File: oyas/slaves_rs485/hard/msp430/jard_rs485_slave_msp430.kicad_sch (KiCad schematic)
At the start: 59 parts, among them J1 POWER, J5 Prog MSP, U1 BPC_Alim3_3V, U1 MAX485E, U2 MSP430F1232IDW, Y1 8MHz

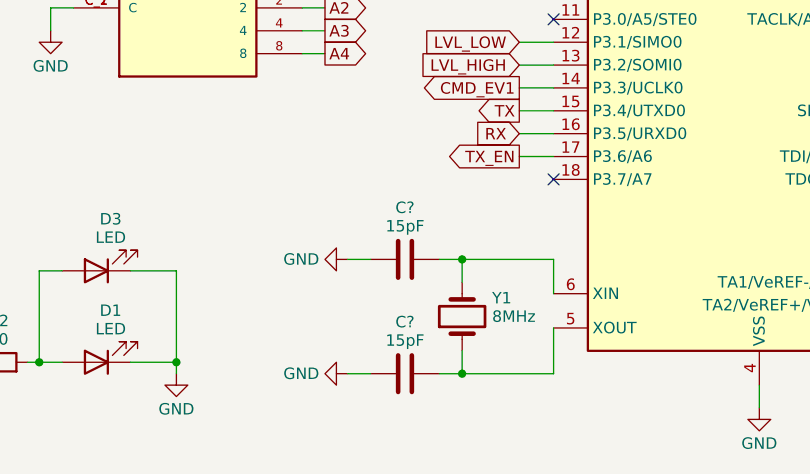
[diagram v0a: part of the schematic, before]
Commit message: Correction valeurs des capas du quartz
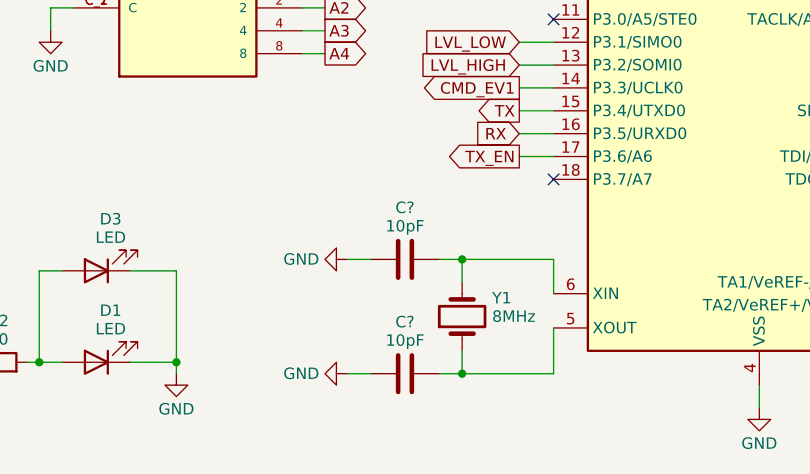
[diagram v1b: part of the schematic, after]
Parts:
- C? (x2): value 15pF -> 10pF
- Y1: Farnel 4235681 -> 4242855; RefFab ABM8AAIG-8.000MHZ-V2R-T -> ABM8AAIG-8.000MHZ-V2R-T3
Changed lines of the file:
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@@
       (effects (font (size 1.27 1.27)))
     )
-    (property "Value" "15pF" (at 95.25 180.459 90)
+    (property "Value" "10pF" (at 95.25 180.459 90)
       (effects (font (size 1.27 1.27)))
     )
@@
       (effects (font (size 1.27 1.27)) hide)
     )
-    (property "Farnel" "4235681" (at 95.25 177.8 0)
-      (effects (font (size 1.27 1.27)) hide)
-    )
-    (property "RefFab" "ABM8AAIG-8.000MHZ-V2R-T" (at 104.9274 179.848 90)
+    (property "Farnel" "4242855" (at 95.25 177.8 0)
+      (effects (font (size 1.27 1.27)) hide)
+    )
+    (property "RefFab" "ABM8AAIG-8.000MHZ-V2R-T3" (at 104.9274 179.848 90)
       (effects (font (size 1.27 1.27)) (justify right) hide)
     )
@@
       (effects (font (size 1.27 1.27)))
     )
-    (property "Value" "15pF" (at 95.25 167.759 90)
-      (effects (font (size 1.27 1.27)))
-    )
+    (property "Value" "10pF" (at 95.25 167.759 90)
+      (effects (font (size 1.27 1.27)))
+    )

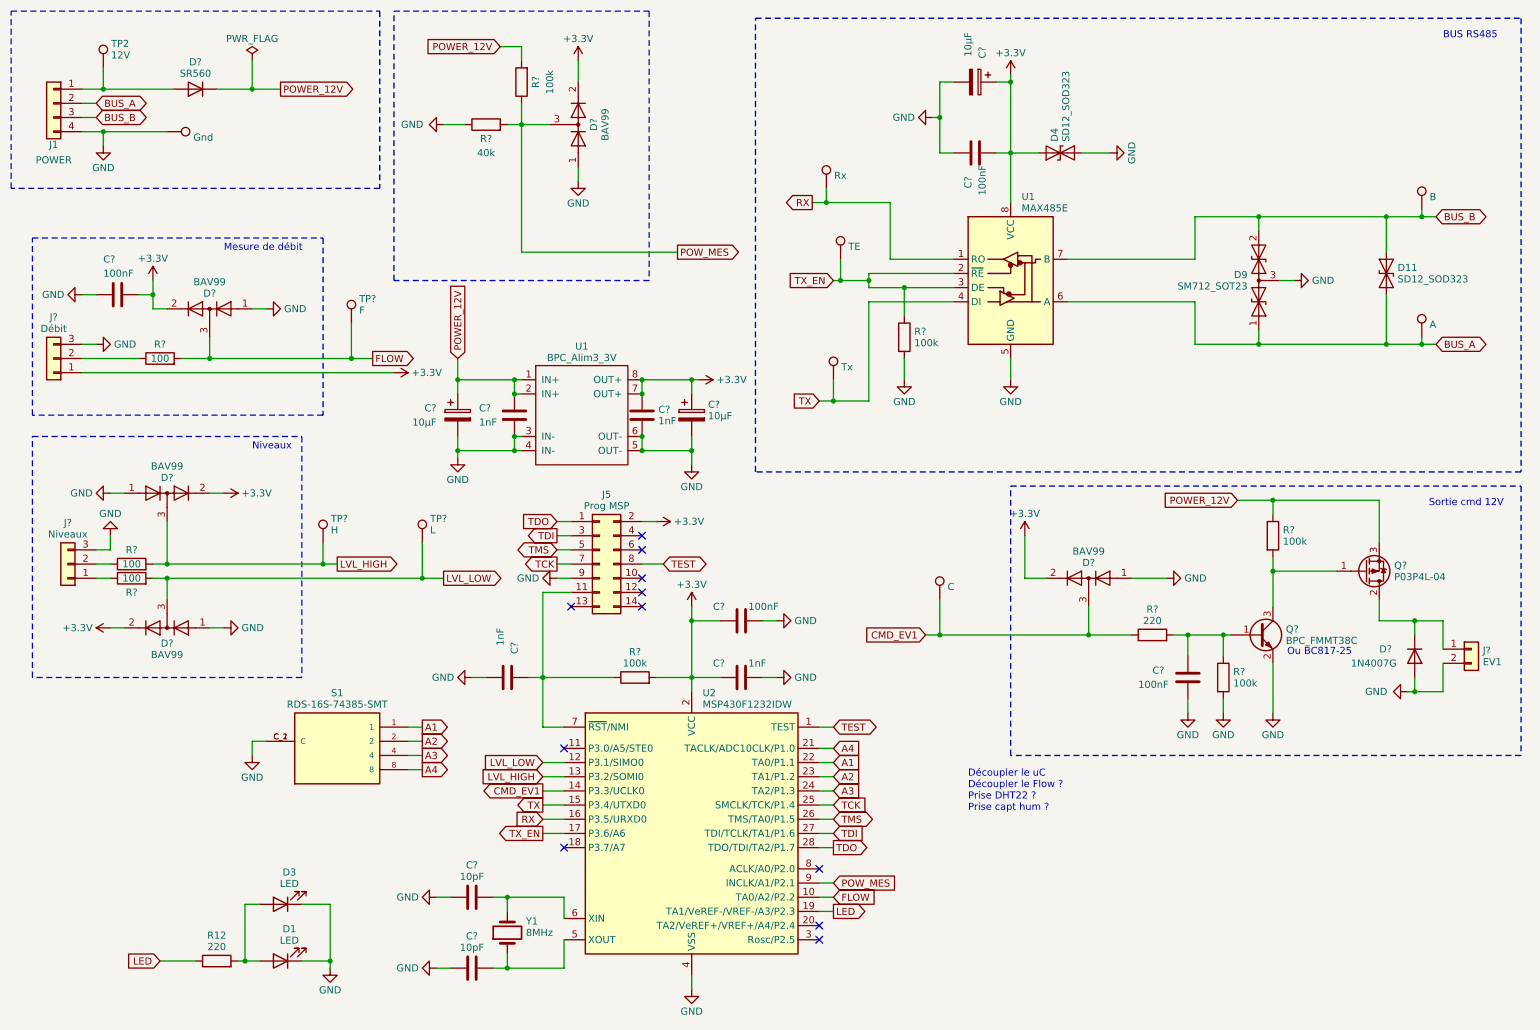
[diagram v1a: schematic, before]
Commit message: Corrections sur la carte Rev A MSP430
- Pas de pullup interne ds MSP430
- Correction sérigraphie et empreinte connecteur de PROG
- Décalage LED
- Suppression de l'entrée débit
- Empreinte des doides TVS et des capas pour être soudables à la main
- Empreinte D12 horizontale
- C8 et C10 en 805 au lieu de 603
- Grossissement de la sérigraphie de version
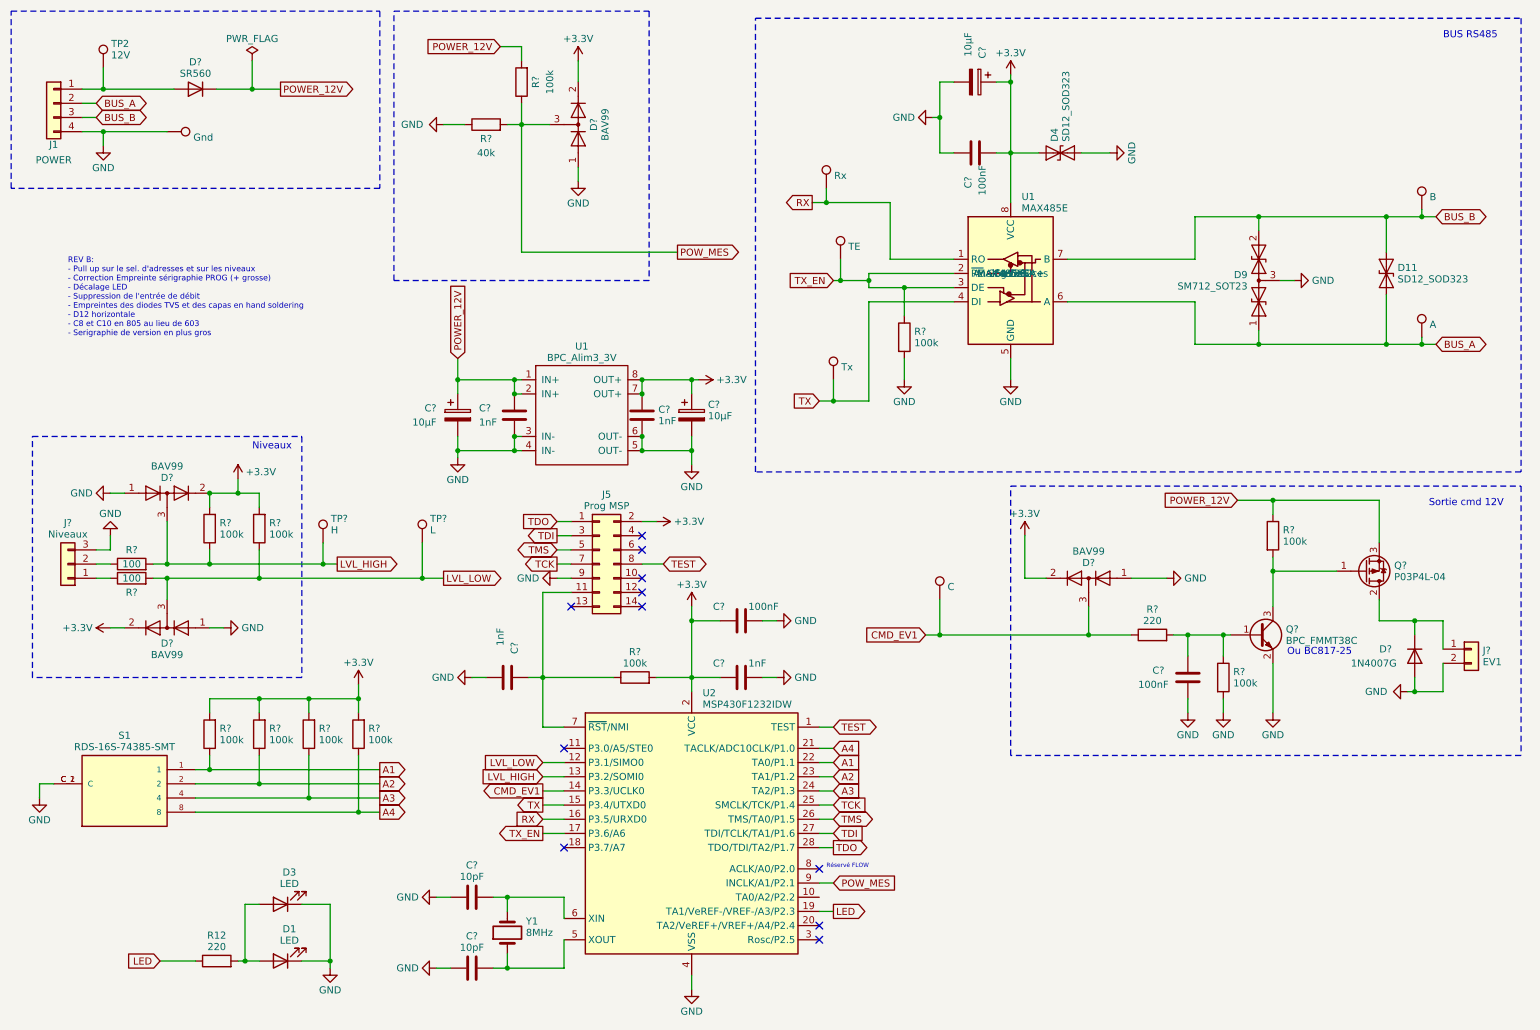
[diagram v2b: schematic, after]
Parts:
- removed C?: 100nF, Capacitor_SMD:C_0805_2012Metric, symbol Device:C
- removed D?: BAV99, Package_TO_SOT_SMD:SOT-23, symbol Diode:BAV99
- removed J?: Débit, TerminalBlock_Phoenix:TerminalBlock_Phoenix_MPT-0,5-3-2.54_1x03_P2.54mm_Horizontal, symbol Connector_Generic:Conn_01x03
- removed R?: 100, Resistor_SMD:R_0805_2012Metric_Pad1.20x1.40mm_HandSolder, symbol Device:R
- removed TP?: F, TestPoint:TestPoint_Pad_D1.0mm, symbol Connector:TestPoint
- added R? (x6): 100k, Resistor_SMD:R_0805_2012Metric_Pad1.20x1.40mm_HandSolder, symbol Device:R
- C? (x6): footprint Capacitor_SMD:C_0805_2012Metric -> Capacitor_SMD:C_0805_2012Metric_Pad1.18x1.45mm_HandSolder
- C? (x2): footprint Capacitor_SMD:C_0603_1608Metric -> Capacitor_SMD:C_0805_2012Metric_Pad1.18x1.45mm_HandSolder
- D11, D4: footprint Diode_SMD:D_SOD-323 -> Diode_SMD:D_SOD-323_HandSoldering
- D?: footprint Diode_THT:D_A-405_P5.08mm_Vertical_KathodeUp -> Diode_THT:D_A-405_P7.62mm_Horizontal
- S1: Price 2,76 -> None
- U1: Fabricant (none) -> Analog Devices; Fournisseur (none) -> Farnell; RefFabricant (none) -> MAX485ESA+; RefFournisseur (none) -> 2519382
- Y1: Fabricant (none) -> Abracon; Fournisseur (none) -> Farnell; RefFabricant (none) -> ABM8AAIG-8.000MHZ-V2R-T3; RefFournisseur (none) -> 4242855
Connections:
- net +3.3V: now also R?.2, R?.2, R?.2, R?.2, R?.2, R?.2
- net A1: now also R?.1
- net A2: now also R?.1
- net A3: now also R?.1
- net A4: now also R?.1
- net LVL_HIGH: now also R?.1
- net LVL_LOW: now also R?.1
- net FLOW: no longer names the net of U2.10 (TA0/A2/P2.2)
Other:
- note added: "REV B: - Pull up sur le sel. d'adresses et sur les niveaux - Correction Empreinte sérigraphie PROG (+ grosse) - Décalage LED - Suppression de l'entrée de débit - Empreintes des diodes TVS et des capas en hand soldering - D12 horizontale - C8 et C10 en 805 au lieu de 603 - Serigraphie de version en plus gros"
- note added: "Réservé FLOW"
- note removed: "Découpler le uC Découpler le Flow ? Prise DHT22 ? Prise capt hum ?"
- note removed: "Mesure de débit"
- moved on the sheet: S1

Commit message: Vérification du nouveau design (Rev B)
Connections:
- no-connect marks 11 -> 12
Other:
- note added: "P2.2: Réservé FLOW"
- note removed: "Réservé FLOW"
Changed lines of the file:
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@@
   (title_block
     (title "Esclave Oya MSP430")
-    (date "2025-04-11")
+    (date "2025-04-13")
     (rev "Rev B")
     (company "BPC")
@@
   (junction (at 264.16 121.92) (diameter 0) (color 0 0 0 0)
   )
+  (no_connect (at 157.48 171.45))
   (no_connect (at 125.73 109.22))
   (no_connect (at 157.48 166.37))
@@
     (effects (font (size 1.27 1.27)) (justify left bottom))
   )
-  (text "Réservé FLOW" (at 158.75 166.37 0)
+  (text "P2.2: Réservé FLOW" (at 165.1 172.72 0)
     (effects (font (size 0.762 0.762)) (justify left bottom))
   )

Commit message: Finitions + Revérification
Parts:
- D11, D4: footprint Diode_SMD:D_SOD-323_HandSoldering -> Diode_SMD:D_SOD-323
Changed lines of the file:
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@@
       (effects (font (size 1.27 1.27)) (justify right))
     )
-    (property "Footprint" "Diode_SMD:D_SOD-323_HandSoldering" (at 264.16 59.69 0)
+    (property "Footprint" "Diode_SMD:D_SOD-323" (at 264.16 59.69 0)
       (effects (font (size 1.27 1.27)) hide)
     )
@@
       (effects (font (size 1.27 1.27)) (justify left))
     )
-    (property "Footprint" "Diode_SMD:D_SOD-323_HandSoldering" (at 200.66 43.18 0)
-      (effects (font (size 1.27 1.27)) hide)
-    )
+    (property "Footprint" "Diode_SMD:D_SOD-323" (at 200.66 43.18 0)
+      (effects (font (size 1.27 1.27)) hide)
+    )

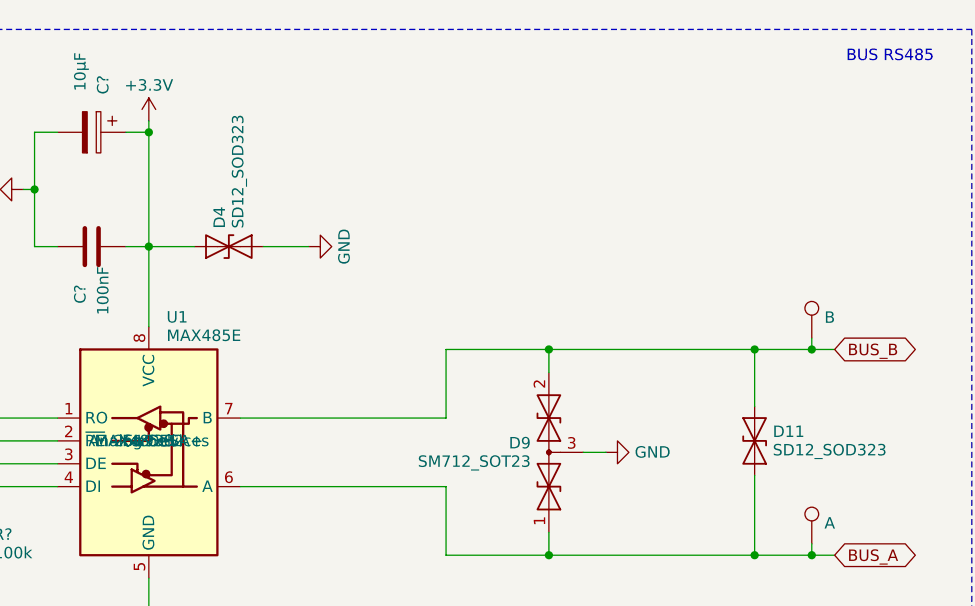
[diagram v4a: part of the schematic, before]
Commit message: Empreinte TVS
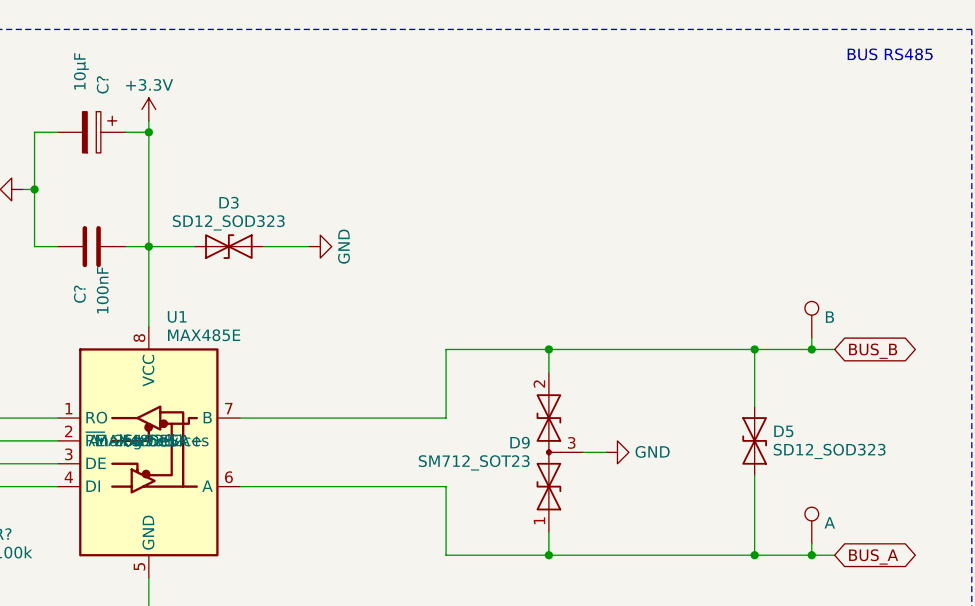
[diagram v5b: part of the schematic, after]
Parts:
- removed D11, D4: SD12_SOD323, Diode_SMD:D_SOD-323, symbol Diode:SD12_SOD323
- added D3, D5: SD12_SOD323, bpc:BPC_D_SOD-323_HandSoldering, symbol bpc:BPC_SD12_SOD323
- C? (x2): footprint Capacitor_SMD:C_0603_1608Metric -> Capacitor_SMD:C_0603_1608Metric_Pad1.08x0.95mm_HandSolder
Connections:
- net +3.3V: now also D3.1 (A1)
- net BUS_A: now also D5.1 (A1)
- net BUS_B: now also D5.2 (A2)
- net GND: now also D3.2 (A2)
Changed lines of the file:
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@@
-    )
-  )
-  (symbol (lib_id "Diode:SD12_SOD323") (at 259.08 59.69 90) (unit 1)
-    (in_bom yes) (on_board yes) (dnp no) (fields_autoplaced)
-    (property "Reference" "D11" (at 261.0866 58.666 90)
-      (effects (font (size 1.27 1.27)) (justify right))
-    )
-    (property "Value" "SD12_SOD323" (at 261.0866 60.714 90)
-      (effects (font (size 1.27 1.27)) (justify right))
-    )
-    (property "Footprint" "Diode_SMD:D_SOD-323" (at 264.16 59.69 0)
-      (effects (font (size 1.27 1.27)) hide)
-    )
-    (property "Datasheet" "https://www.littelfuse.com/~/media/electronics/datasheets/tvs_diode_arrays/littelfuse_tvs_diode_array_sd_c_datasheet.pdf.pdf" (at 259.08 59.69 0)
-      (effects (font (size 1.27 1.27)) hide)
-    )
-    (property "RefFabricant" "SD12-7" (at 259.08 59.69 0)
-      (effects (font (size 1.27 1.27)) hide)
-    )
-    (property "RefFournisseur" "3945781RL" (at 259.08 59.69 0)
-      (effects (font (size 1.27 1.27)) hide)
-    )
-    (property "Fabricant" "DIODES INC" (at 259.08 59.69 0)
-      (effects (font (size 1.27 1.27)) hide)
-    )
-    (property "Fournisseur" "Farnell" (at 259.08 59.69 0)
-      (effects (font (size 1.27 1.27)) hide)
-    )
-    (property "Description" "Diodes TVS simples" (at 259.08 59.69 0)
-      (effects (font (size 1.27 1.27)) hide)
-    )
-    (property "Price" "0,1272" (at 259.08 59.69 0)
-      (effects (font (size 1.27 1.27)) hide)
-    )
-    (pin "1")
-    (pin "2")
-    (instances
-      (project "jard_rs485_slave_mods2"
-        (path "/5ae93d62-0543-4c0e-b37d-d67af6219e1b/36e9fbeb-2032-4e73-95af-53e316cf916d"
-          (reference "D11") (unit 1)
-        )
-        (path "/5ae93d62-0543-4c0e-b37d-d67af6219e1b/dec80786-a2aa-49f2-be55-5994d7e13863"
-          (reference "D11") (unit 1)
-        )
-      )
-      (project "jard_rs485_slave_msp430"
-        (path "/a198b99e-c4dc-4064-b4d8-b20710c7a061"
-          (reference "D5") (unit 1)
-        )
-      )
     )
   )
@@
     )
   )
+  (symbol (lib_id "bpc:BPC_SD12_SOD323") (at 200.66 38.1 0) (unit 1)
+    (in_bom yes) (on_board yes) (dnp no) (fields_autoplaced)
+    (property "Reference" "D3" (at 200.66 33.2754 0)
+      (effects (font (size 1.27 1.27)))
+    )
+    (property "Value" "SD12_SOD323" (at 200.66 35.3234 0)
+      (effects (font (size 1.27 1.27)))
+    )
+    (property "Footprint" "bpc:BPC_D_SOD-323_HandSoldering" (at 200.66 43.18 0)
+      (effects (font (size 1.27 1.27)) hide)
+    )
+    (property "Datasheet" "https://www.littelfuse.com/~/media/electronics/datasheets/tvs_diode_arrays/littelfuse_tvs_diode_array_sd_c_datasheet.pdf.pdf" (at 200.66 38.1 0)
+      (effects (font (size 1.27 1.27)) hide)
+    )
+    (pin "1")
+    (pin "2")
+    (instances
+      (project "jard_rs485_slave_msp430"
+        (path "/a198b99e-c4dc-4064-b4d8-b20710c7a061"
+          (reference "D3") (unit 1)
+        )
+      )
+    )
+  )
   (symbol (lib_id "Device:C") (at 95.25 184.15 90) (unit 1)
     (in_bom yes) (on_board yes) (dnp no) (fields_autoplaced)
@@
       (effects (font (size 1.27 1.27)))
     )
-    (property "Footprint" "Capacitor_SMD:C_0603_1608Metric" (at 99.06 183.1848 0)
+    (property "Footprint" "Capacitor_SMD:C_0603_1608Metric_Pad1.08x0.95mm_HandSolder" (at 99.06 183.1848 0)
       (effects (font (size 1.27 1.27)) hide)
     )
@@
       (effects (font (size 1.27 1.27)))
     )
-    (property "Footprint" "Capacitor_SMD:C_0603_1608Metric" (at 99.06 170.4848 0)
+    (property "Footprint" "Capacitor_SMD:C_0603_1608Metric_Pad1.08x0.95mm_HandSolder" (at 99.06 170.4848 0)
       (effects (font (size 1.27 1.27)) hide)
     )
@@
     )
   )
-  (symbol (lib_id "Diode:SD12_SOD323") (at 200.66 38.1 0) (unit 1)
-    (in_bom yes) (on_board yes) (dnp no) (fields_autoplaced)
-    (property "Reference" "D4" (at 199.636 36.0934 90)
-      (effects (font (size 1.27 1.27)) (justify left))
-    )
-    (property "Value" "SD12_SOD323" (at 201.684 36.0934 90)
-      (effects (font (size 1.27 1.27)) (justify left))
-    )
-    (property "Footprint" "Diode_SMD:D_SOD-323" (at 200.66 43.18 0)
-      (effects (font (size 1.27 1.27)) hide)
-    )
-    (property "Datasheet" "https://www.littelfuse.com/~/media/electronics/datasheets/tvs_diode_arrays/littelfuse_tvs_diode_array_sd_c_datasheet.pdf.pdf" (at 200.66 38.1 0)
-      (effects (font (size 1.27 1.27)) hide)
-    )
-    (property "RefFabricant" "SD12-7" (at 200.66 38.1 0)
-      (effects (font (size 1.27 1.27)) hide)
-    )
-    (property "RefFournisseur" "3945781RL" (at 200.66 38.1 0)
-      (effects (font (size 1.27 1.27)) hide)
-    )
-    (property "Fabricant" "DIODES INC" (at 200.66 38.1 0)
-      (effects (font (size 1.27 1.27)) hide)
-    )
-    (property "Fournisseur" "Farnell" (at 200.66 38.1 0)
-      (effects (font (size 1.27 1.27)) hide)
-    )
-    (property "Description" "Diodes TVS simples" (at 200.66 38.1 0)
-      (effects (font (size 1.27 1.27)) hide)
-    )
-    (property "Price" "0,1272" (at 200.66 38.1 0)
-      (effects (font (size 1.27 1.27)) hide)
-    )
-    (pin "1")
-    (pin "2")
-    (instances
-      (project "jard_rs485_slave_mods2"
-        (path "/5ae93d62-0543-4c0e-b37d-d67af6219e1b/36e9fbeb-2032-4e73-95af-53e316cf916d"
-          (reference "D4") (unit 1)
-        )
-        (path "/5ae93d62-0543-4c0e-b37d-d67af6219e1b/dec80786-a2aa-49f2-be55-5994d7e13863"
-          (reference "D4") (unit 1)
-        )
-      )
-      (project "jard_rs485_slave_msp430"
-        (path "/a198b99e-c4dc-4064-b4d8-b20710c7a061"
-          (reference "D3") (unit 1)
-        )
-      )
+  (symbol (lib_id "bpc:BPC_SD12_SOD323") (at 259.08 59.69 90) (unit 1)
+    (in_bom yes) (on_board yes) (dnp no) (fields_autoplaced)
+    (property "Reference" "D5" (at 261.0866 58.666 90)
+      (effects (font (size 1.27 1.27)) (justify right))
+    )
+    (property "Value" "SD12_SOD323" (at 261.0866 60.714 90)
+      (effects (font (size 1.27 1.27)) (justify right))
+    )
+    (property "Footprint" "bpc:BPC_D_SOD-323_HandSoldering" (at 264.16 59.69 0)
+      (effects (font (size 1.27 1.27)) hide)
+    )
+    (property "Datasheet" "https://www.littelfuse.com/~/media/electronics/datasheets/tvs_diode_arrays/littelfuse_tvs_diode_array_sd_c_datasheet.pdf.pdf" (at 259.08 59.69 0)
+      (effects (font (size 1.27 1.27)) hide)
+    )
+    (pin "1")
+    (pin "2")
+    (instances
+      (project "jard_rs485_slave_msp430"
+        (path "/a198b99e-c4dc-4064-b4d8-b20710c7a061"
+          (reference "D5") (unit 1)
+        )
+      )
